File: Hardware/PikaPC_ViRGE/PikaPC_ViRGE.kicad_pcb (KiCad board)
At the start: 4 copper layers, 101.6 x 101.6 mm, 170 parts, among them J1 DIN41612_03x32_C_Split, J2 Conn_02x07_Odd_Even, J3 Conn_02x08_Odd_Even, J4 DE15_Socket_HighDensity_Mount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, U1 86C325, U10 74AHCT573, U12 74FCT2245, U13 74FCT2245, U14 74FCT2245, U15 74FCT2245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

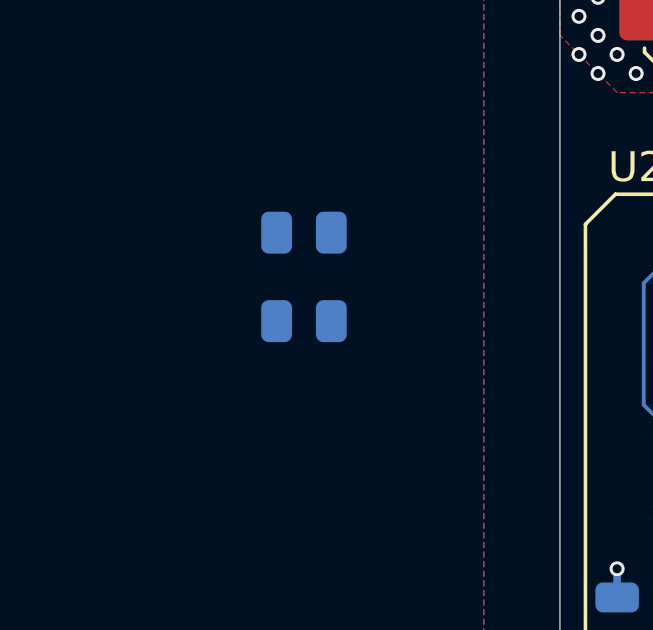
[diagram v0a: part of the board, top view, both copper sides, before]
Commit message: Add pull-up to LOCA# on ViRGE card
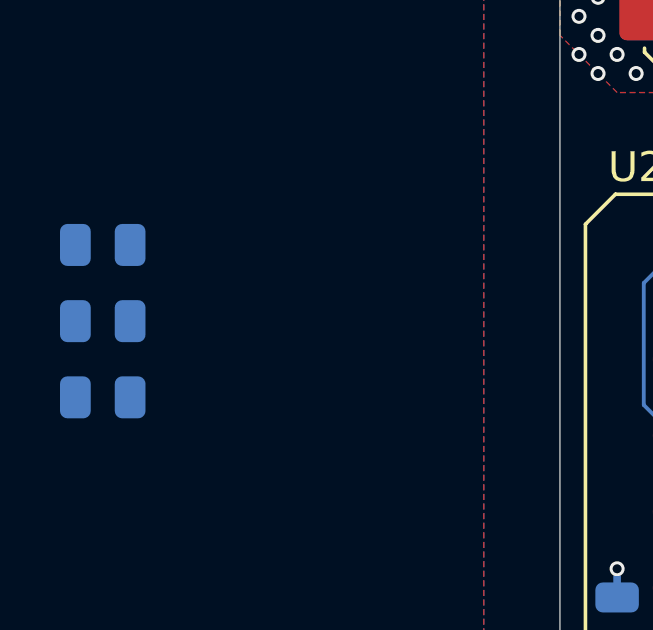
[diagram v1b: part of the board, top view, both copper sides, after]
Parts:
- added R41: 10K, Resistor_SMD:R_0805_2012Metric, B.Cu at (61.0, 76.2)
- moved R40 6.72 mm to (61.0, 71.1)
- moved R39 6.71 mm to (61.0, 73.7)
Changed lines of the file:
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@@
 	(footprint "Resistor_SMD:R_0805_2012Metric"
 		(layer "B.Cu")
-		(at 67.6675 73.66)
+		(at 60.96 73.66)
 		(descr "Resistor SMD 0805 (2012 Metric), square (rectangular) end terminal, IPC-7351 nominal, (Body size source: IPC-SM-782 page 72, https://www.pcb-3d.com/wordpress/wp-content/uploads/ipc-sm-782a_amendment_1_and_2.pdf), generated with kicad-footprint-generator")
 		(tags "resistor")
@@
 	(footprint "Resistor_SMD:R_0805_2012Metric"
 		(layer "B.Cu")
-		(at 67.6675 70.71)
+		(at 60.96 71.12)
 		(descr "Resistor SMD 0805 (2012 Metric), square (rectangular) end terminal, IPC-7351 nominal, (Body size source: IPC-SM-782 page 72, https://www.pcb-3d.com/wordpress/wp-content/uploads/ipc-sm-782a_amendment_1_and_2.pdf), generated with kicad-footprint-generator")
 		(tags "resistor")
@@
 			(pintype "passive")
 		)
+		(embedded_fonts no)
+		(model "${KICAD9_3DMODEL_DIR}/Resistor_SMD.3dshapes/R_0805_2012Metric.step"
+			(offset
+				(xyz 0 0 0)
+			)
+			(scale
+				(xyz 1 1 1)
+			)
+			(rotate
+				(xyz 0 0 0)
+			)
+		)
+	)
+	(footprint "Resistor_SMD:R_0805_2012Metric"
+		(layer "B.Cu")
+		(at 60.96 76.2)
+		(descr "Resistor SMD 0805 (2012 Metric), square (rectangular) end terminal, IPC-7351 nominal, (Body size source: IPC-SM-782 page 72, https://www.pcb-3d.com/wordpress/wp-content/uploads/ipc-sm-782a_amendment_1_and_2.pdf), generated with kicad-footprint-generator")
+		(tags "resistor")
+		(property "Reference" "R41"
+			(at 0 1.65 180)
+			(layer "B.SilkS")
+			(effects
+				(font
+					(size 1 1)
+					(thickness 0.15)
+				)
+				(justify mirror)
+			)
+		)
+		(property "Value" "10K"
+			(at 0 -1.65 180)
+			(layer "B.Fab")
+			(effects
+				(font
+					(size 1 1)
+					(thickness 0.15)
+				)
+				(justify mirror)
+			)
+		)
+		(property "Datasheet" ""
+			(at 0 0 180)
+			(layer "B.Fab")
+			(hide yes)
+			(effects
+				(font
+					(size 1.27 1.27)
+					(thickness 0.15)
+				)
+				(justify mirror)
+			)
+		)
+		(property "Description" ""
+			(at 0 0 180)
+			(layer "B.Fab")
+			(hide yes)
+			(effects
+				(font
+					(size 1.27 1.27)
+					(thickness 0.15)
+				)
+				(justify mirror)
+			)
+		)
+		(property "Mouser" "303-0805S8J0103T5E "
+			(at 0 0 180)
+			(unlocked yes)
+			(layer "B.Fab")
+			(hide yes)
+			(effects
+				(font
+					(size 1 1)
+					(thickness 0.15)
+				)
+				(justify mirror)
+			)
+		)
+		(property ki_fp_filters "R_*")
+		(sheetname "/Main Bus/")
+		(sheetfile "main_bus.kicad_sch")
+		(attr smd)
+		(fp_line
+			(start -0.227064 -0.735)
+			(end 0.227064 -0.735)
+			(stroke
+				(width 0.12)
+				(type solid)
+			)
+			(layer "B.SilkS")
+		)
+		(fp_line
+			(start -0.227064 0.735)
+			(end 0.227064 0.735)
+			(stroke
+				(width 0.12)
+				(type solid)
+			)
+			(layer "B.SilkS")
+		)
+		(fp_line
+			(start -1.68 -0.95)
+			(end -1.68 0.95)
+			(stroke
+				(width 0.05)
+				(type solid)
+			)
+			(layer "B.CrtYd")
+		)
+		(fp_line
+			(start -1.68 0.95)
+			(end 1.68 0.95)
+			(stroke
+				(width 0.05)
+				(type solid)
+			)
+			(layer "B.CrtYd")
+		)
+		(fp_line
+			(start 1.68 -0.95)
+			(end -1.68 -0.95)
+			(stroke
+				(width 0.05)
+				(type solid)
+			)
+			(layer "B.CrtYd")
+		)
+		(fp_line
+			(start 1.68 0.95)
+			(end 1.68 -0.95)
+			(stroke
+				(width 0.05)
+				(type solid)
+			)
+			(layer "B.CrtYd")
+		)
+		(fp_line
+			(start -1 -0.625)
+			(end -1 0.625)
+			(stroke
+				(width 0.1)
+				(type solid)
+			)
+			(layer "B.Fab")
+		)
+		(fp_line
+			(start -1 0.625)
+			(end 1 0.625)
+			(stroke
+				(width 0.1)
+				(type solid)
+			)
+			(layer "B.Fab")
+		)
+		(fp_line
+			(start 1 -0.625)
+			(end -1 -0.625)
+			(stroke
+				(width 0.1)
+				(type solid)
+			)
+			(layer "B.Fab")
+		)
+		(fp_line
+			(start 1 0.625)
+			(end 1 -0.625)
+			(stroke
+				(width 0.1)
+				(type solid)
+			)
+			(layer "B.Fab")
+		)
+		(fp_text user "${REFERENCE}"
+			(at 0 0 180)
+			(layer "B.Fab")
+			(effects
+				(font
+					(size 0.5 0.5)
+					(thickness 0.08)
+				)
+				(justify mirror)
+			)
+		)
+		(pad "1" smd roundrect
+			(at -0.9125 0)
+			(size 1.025 1.4)
+			(layers "B.Cu" "B.Mask" "B.Paste")
+			(roundrect_rratio 0.243902)
+			(net 204 "/Main Bus/~{VID-LOCA}")
+			(pintype "passive")
+		)
+		(pad "2" smd roundrect
+			(at 0.9125 0)
+			(size 1.025 1.4)
+			(layers "B.Cu" "B.Mask" "B.Paste")
+			(roundrect_rratio 0.243902)
+			(net 2 "+5V")
+			(pintype "passive")
+		)
